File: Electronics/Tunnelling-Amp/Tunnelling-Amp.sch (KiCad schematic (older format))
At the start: 15 parts, among them J1 RF_Shield_Two_Pieces, U1 ADA4627-1

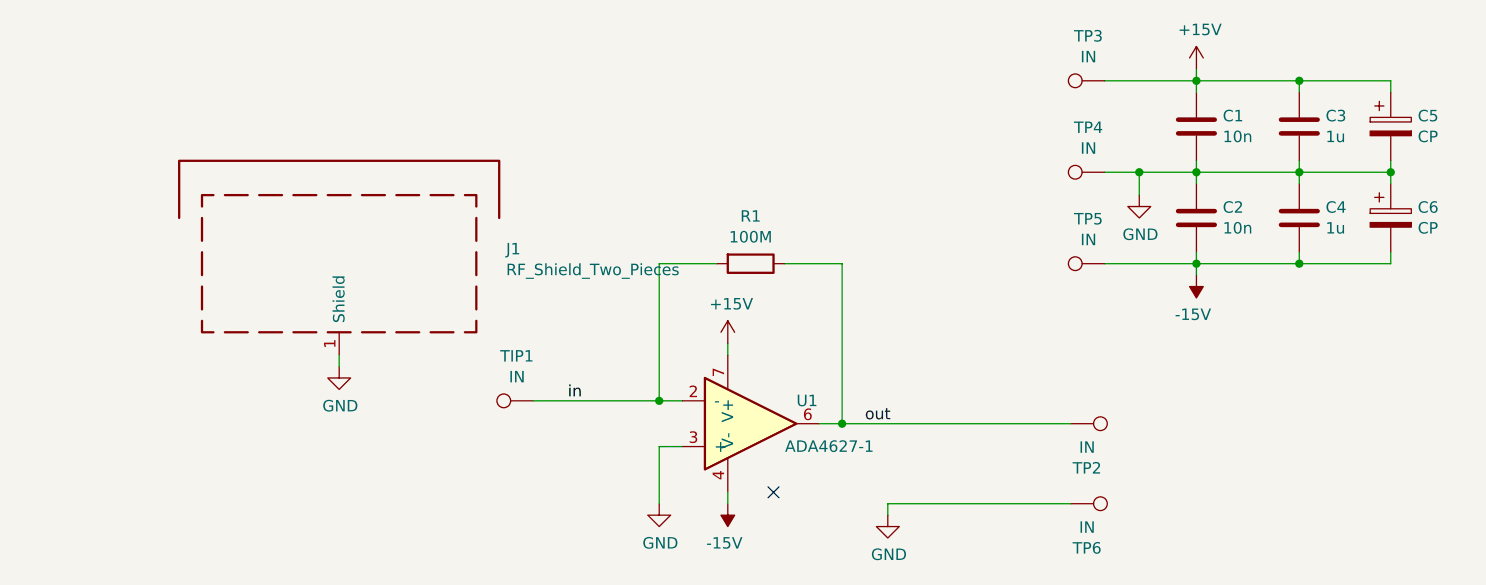
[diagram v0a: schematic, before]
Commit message: Supply board and tunneling amp finished
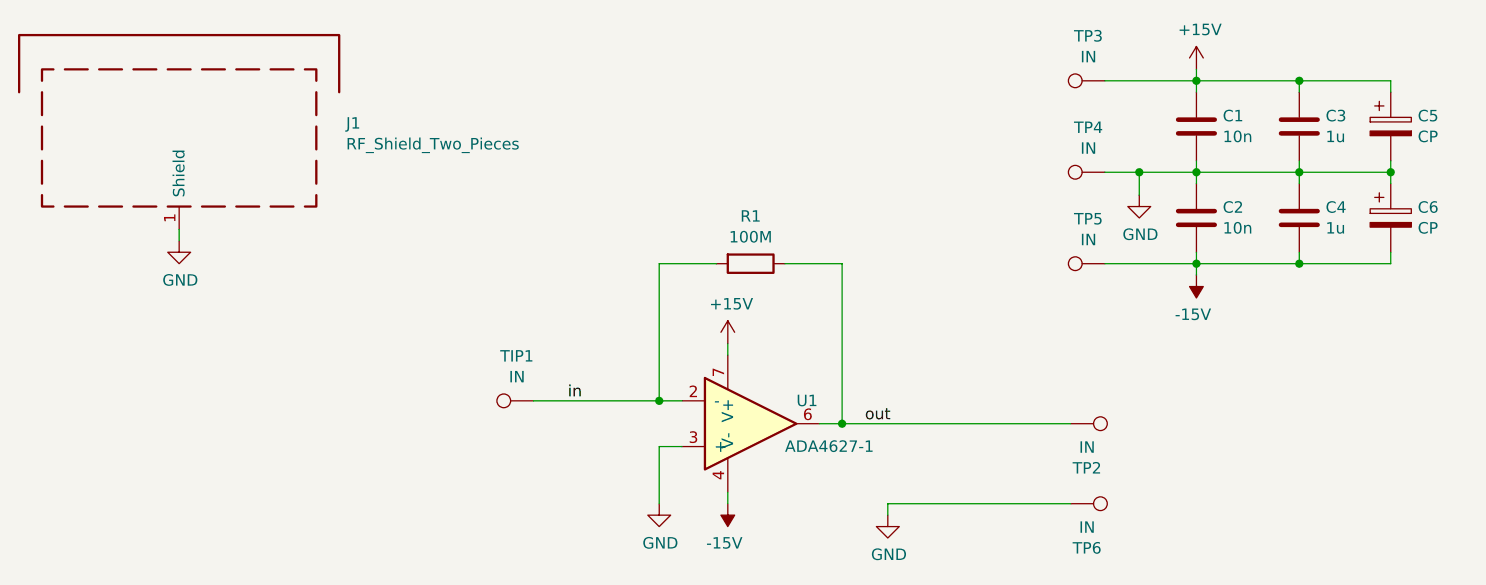
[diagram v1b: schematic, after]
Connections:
- no-connect marks 1 -> 0
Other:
- moved on the sheet: J1
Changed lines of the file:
@@
 EESchema Schematic File Version 4
 LIBS:Tunnelling-Amp-cache
-EELAYER 29 0
+EELAYER 30 0
 EELAYER END
 $Descr A4 11693 8268
@@
 Wire Wire Line
 	5400 4250 5400 4200
-NoConn ~ 5600 4200
 $Comp
 L power:GND #PWR01
@@
 L Device:RF_Shield_Two_Pieces J1
 U 1 1 5D3A9A3E
-P 3700 3200
-F 0 "J1" H 4430 3264 50  0000 L CNN
-F 1 "RF_Shield_Two_Pieces" H 4430 3173 50  0000 L CNN
-F 2 "RF_Shielding:Laird_Technologies_BMI-S-101_13.66x12.70mm" H 3700 3100 50  0001 C CNN
-F 3 "~" H 3700 3100 50  0001 C CNN
-	1    3700 3200
+P 3000 2650
+F 0 "J1" H 3730 2714 50  0000 L CNN
+F 1 "RF_Shield_Two_Pieces" H 3730 2623 50  0000 L CNN
+F 2 "RF_Shielding:Laird_Technologies_BMI-S-101_13.66x12.70mm" H 3000 2550 50  0001 C CNN
+F 3 "~" H 3000 2550 50  0001 C CNN
+	1    3000 2650
 	1    0    0    -1
 $EndComp
@@
 L power:GND #PWR0101
 U 1 1 5D3AEB62
-P 3700 3650
-F 0 "#PWR0101" H 3700 3400 50  0001 C CNN
-F 1 "GND" H 3705 3477 50  0000 C CNN
-F 2 "" H 3700 3650 50  0001 C CNN
-F 3 "" H 3700 3650 50  0001 C CNN
-	1    3700 3650
-	1    0    0    -1
-$EndComp
-Wire Wire Line
-	3700 3650 3700 3600
+P 3000 3100
+F 0 "#PWR0101" H 3000 2850 50  0001 C CNN
+F 1 "GND" H 3005 2927 50  0000 C CNN
+F 2 "" H 3000 3100 50  0001 C CNN
+F 3 "" H 3000 3100 50  0001 C CNN
+	1    3000 3100
+	1    0    0    -1
+$EndComp
+Wire Wire Line
+	3000 3100 3000 3050
 Connection ~ 5900 3900
 $Comp

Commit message: Added images
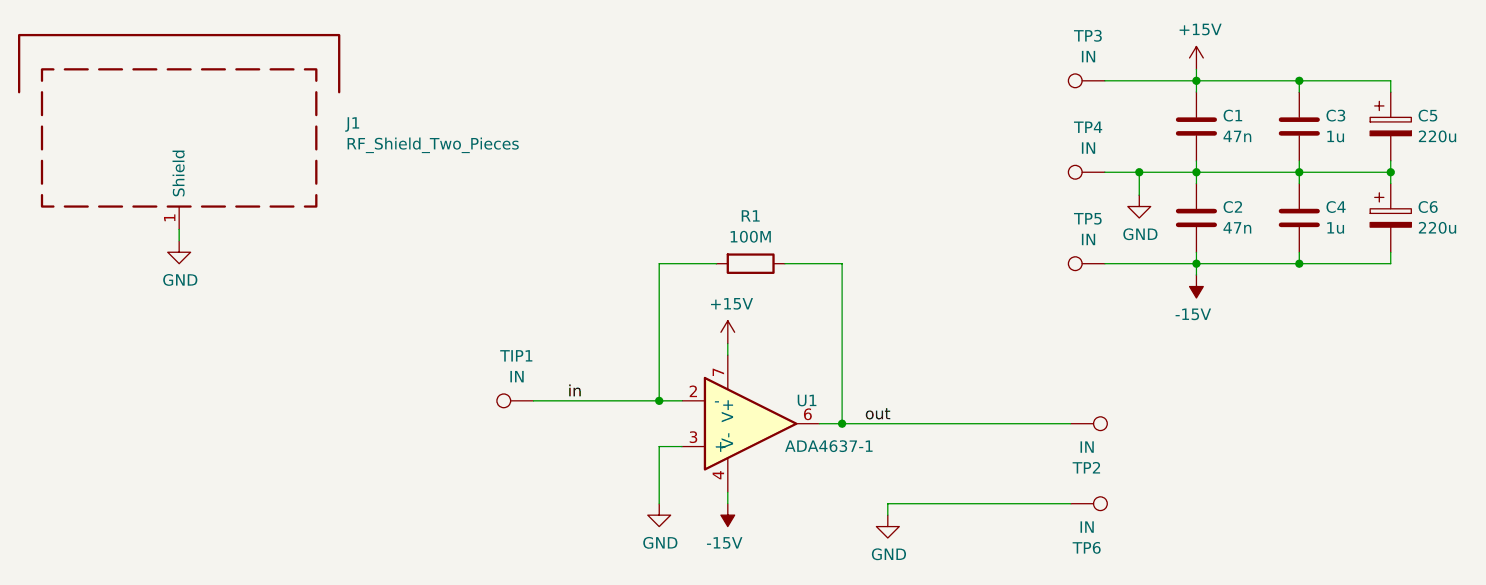
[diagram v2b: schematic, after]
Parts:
- C1, C2: value 10n -> 47n; Reichelt (none) -> KEM X7R0603 47N
- C3, C4: Reichelt (none) -> X7R-G0805 1,0/50
- C5, C6: value CP -> 220u; Reichelt (none) -> ELN RV2-35V220MU
- J1: Digikey (none) -> 903-1006-1-ND
- R1: Digikey (none) -> 541-100MALCT-ND
- U1: value ADA4627-1 -> ADA4637-1; Digikey (none) -> ADA4637-1ARZ-ND
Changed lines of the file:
@@
 EESchema Schematic File Version 4
-LIBS:Tunnelling-Amp-cache
 EELAYER 30 0
 EELAYER END
@@
 P 5500 3900
 F 0 "U1" H 5700 4000 50  0000 L CNN
-F 1 "ADA4627-1" H 5650 3800 50  0000 L CNN
+F 1 "ADA4637-1" H 5650 3800 50  0000 L CNN
 F 2 "custom:SOIC-8_3.9x4.9mm_P1.27mm" H 5700 4150 50  0001 C CNN
 F 3 "" H 5700 4150 50  0001 C CNN
+F 4 "ADA4637-1ARZ-ND" H 5500 3900 50  0001 C CNN "Digikey"
 	1    5500 3900
 	1    0    0    -1
@@
 P 7450 2600
 F 0 "C1" H 7565 2646 50  0000 L CNN
-F 1 "10n" H 7565 2555 50  0000 L CNN
+F 1 "47n" H 7565 2555 50  0000 L CNN
 F 2 "Capacitor_SMD:C_0603_1608Metric_Pad1.05x0.95mm_HandSolder" H 7488 2450 50  0001 C CNN
 F 3 "~" H 7450 2600 50  0001 C CNN
+F 4 "KEM X7R0603 47N" H 7450 2600 50  0001 C CNN "Reichelt"
 	1    7450 2600
 	1    0    0    -1
@@
 F 2 "Resistor_SMD:R_1206_3216Metric_Pad1.42x1.75mm_HandSolder" V 5430 3200 50  0001 C CNN
 F 3 "~" H 5500 3200 50  0001 C CNN
+F 4 "541-100MALCT-ND" V 5500 3200 50  0001 C CNN "Digikey"
 	1    5500 3200
 	0    1    1    0
@@
 F 2 "Capacitor_SMD:C_0805_2012Metric_Pad1.15x1.40mm_HandSolder" H 7938 2450 50  0001 C CNN
 F 3 "~" H 7900 2600 50  0001 C CNN
+F 4 "X7R-G0805 1,0/50" H 7900 2600 50  0001 C CNN "Reichelt"
 	1    7900 2600
 	1    0    0    -1
@@
 P 8300 2600
 F 0 "C5" H 8418 2646 50  0000 L CNN
-F 1 "CP" H 8418 2555 50  0000 L CNN
+F 1 "220u" H 8418 2555 50  0000 L CNN
 F 2 "Capacitor_SMD:CP_Elec_6.3x5.4" H 8338 2450 50  0001 C CNN
 F 3 "~" H 8300 2600 50  0001 C CNN
+F 4 "ELN RV2-35V220MU" H 8300 2600 50  0001 C CNN "Reichelt"
 	1    8300 2600
 	1    0    0    -1
@@
 P 7450 3000
 F 0 "C2" H 7565 3046 50  0000 L CNN
-F 1 "10n" H 7565 2955 50  0000 L CNN
+F 1 "47n" H 7565 2955 50  0000 L CNN
 F 2 "Capacitor_SMD:C_0603_1608Metric_Pad1.05x0.95mm_HandSolder" H 7488 2850 50  0001 C CNN
 F 3 "~" H 7450 3000 50  0001 C CNN
+F 4 "KEM X7R0603 47N" H 7450 3000 50  0001 C CNN "Reichelt"
 	1    7450 3000
 	1    0    0    -1
@@
 F 2 "Capacitor_SMD:C_0805_2012Metric_Pad1.15x1.40mm_HandSolder" H 7938 2850 50  0001 C CNN
 F 3 "~" H 7900 3000 50  0001 C CNN
+F 4 "X7R-G0805 1,0/50" H 7900 3000 50  0001 C CNN "Reichelt"
 	1    7900 3000
 	1    0    0    -1
@@
 P 8300 3000
 F 0 "C6" H 8418 3046 50  0000 L CNN
-F 1 "CP" H 8418 2955 50  0000 L CNN
+F 1 "220u" H 8418 2955 50  0000 L CNN
 F 2 "Capacitor_SMD:CP_Elec_6.3x5.4" H 8338 2850 50  0001 C CNN
 F 3 "~" H 8300 3000 50  0001 C CNN
+F 4 "ELN RV2-35V220MU" H 8300 3000 50  0001 C CNN "Reichelt"
 	1    8300 3000
 	1    0    0    -1
@@
 F 2 "RF_Shielding:Laird_Technologies_BMI-S-101_13.66x12.70mm" H 3000 2550 50  0001 C CNN
 F 3 "~" H 3000 2550 50  0001 C CNN
+F 4 "903-1006-1-ND" H 3000 2650 50  0001 C CNN "Digikey"
 	1    3000 2650
 	1    0    0    -1

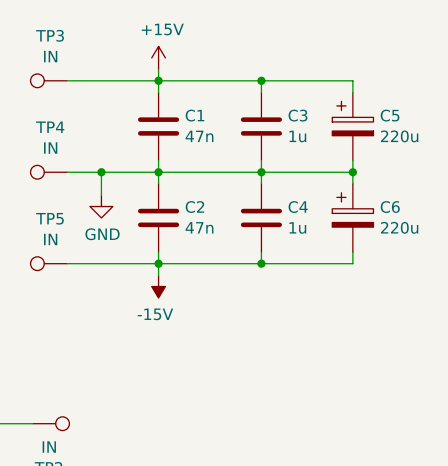
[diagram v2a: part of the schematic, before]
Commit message: Fixed values in schematic
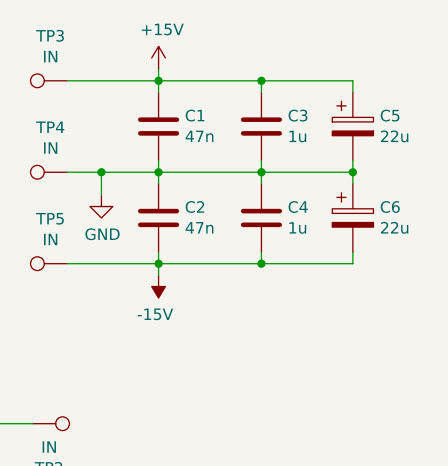
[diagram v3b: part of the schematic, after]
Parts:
- C5, C6: value 220u -> 22u
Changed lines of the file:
@@
 P 8300 2600
 F 0 "C5" H 8418 2646 50  0000 L CNN
-F 1 "220u" H 8418 2555 50  0000 L CNN
+F 1 "22u" H 8418 2555 50  0000 L CNN
 F 2 "Capacitor_SMD:CP_Elec_6.3x5.4" H 8338 2450 50  0001 C CNN
 F 3 "~" H 8300 2600 50  0001 C CNN
@@
 P 8300 3000
 F 0 "C6" H 8418 3046 50  0000 L CNN
-F 1 "220u" H 8418 2955 50  0000 L CNN
+F 1 "22u" H 8418 2955 50  0000 L CNN
 F 2 "Capacitor_SMD:CP_Elec_6.3x5.4" H 8338 2850 50  0001 C CNN
 F 3 "~" H 8300 3000 50  0001 C CNN
